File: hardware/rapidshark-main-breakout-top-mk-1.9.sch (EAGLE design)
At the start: 10 parts, among them U1 ADAFRUIT_METRO_MININOSILK-AMB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

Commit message: tweaks to jst part hole sizes
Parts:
- F1: value 100mA -> 120mA
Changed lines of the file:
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@@
 <setting verticaltext="up"/>
 </settings>
-<grid distance="100" unitdist="mil" unit="mil" style="lines" multiple="1" display="yes" altdistance="1" altunitdist="mil" altunit="mil"/>
+<grid distance="100" unitdist="mil" unit="mil" style="lines" multiple="1" display="yes" altdistance="2" altunitdist="mil" altunit="mil"/>
 <layers>
 <layer number="1" name="Top" color="4" fill="1" visible="no" active="no"/>
@@
 <part name="SUPPLY16" library="A_butts" deviceset="5V" device=""/>
 <part name="SUPPLY17" library="A_butts" deviceset="3.3V" device=""/>
-<part name="F1" library="A_butts" deviceset="PTC" device="SMD" value="100mA"/>
+<part name="F1" library="A_butts" deviceset="PTC" device="SMD" value="120mA"/>
 <part name="SUPPLY1" library="A_butts" deviceset="5V" device=""/>
 <part name="SUPPLY2" library="A_butts" deviceset="5V" device=""/>

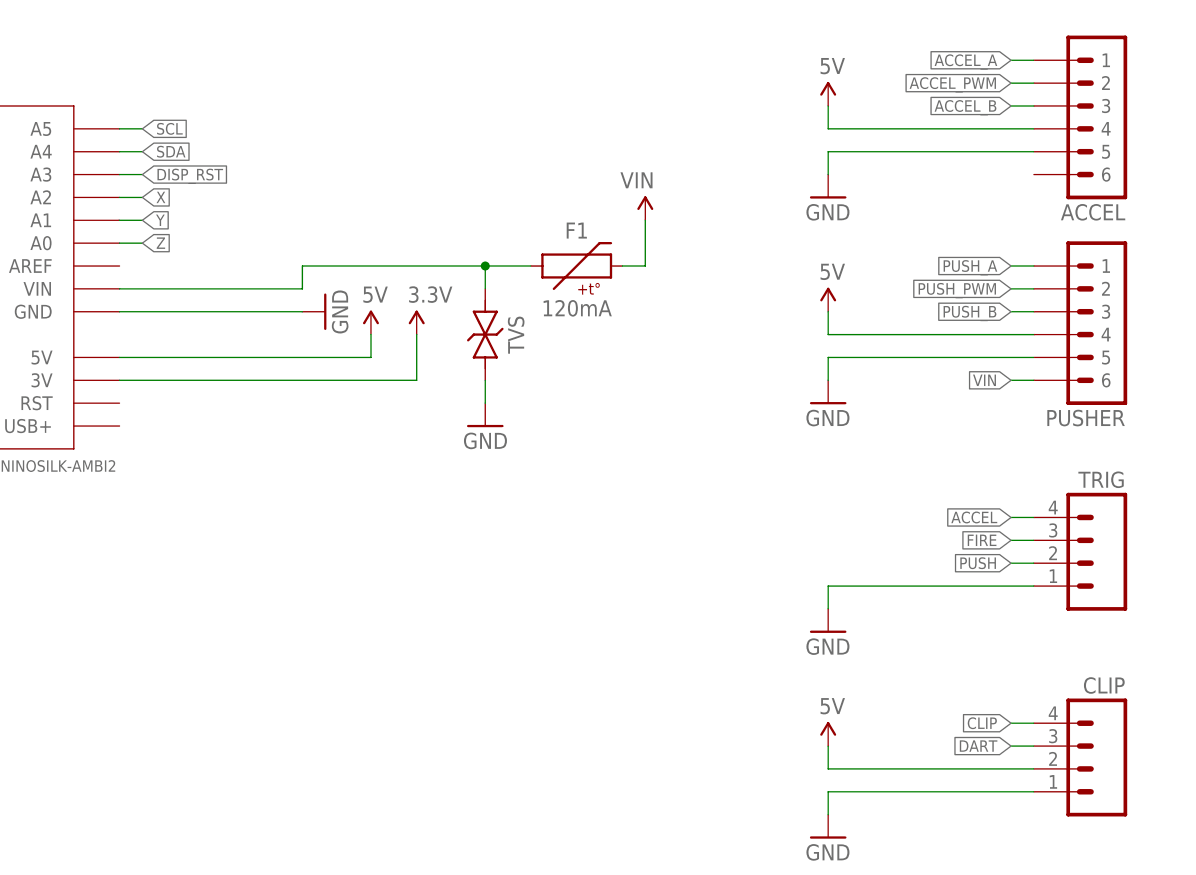
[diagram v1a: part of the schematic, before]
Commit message: relayout and now provides both 3V and 5V to display (but assumes IO voltage is whatever the arduino sends out
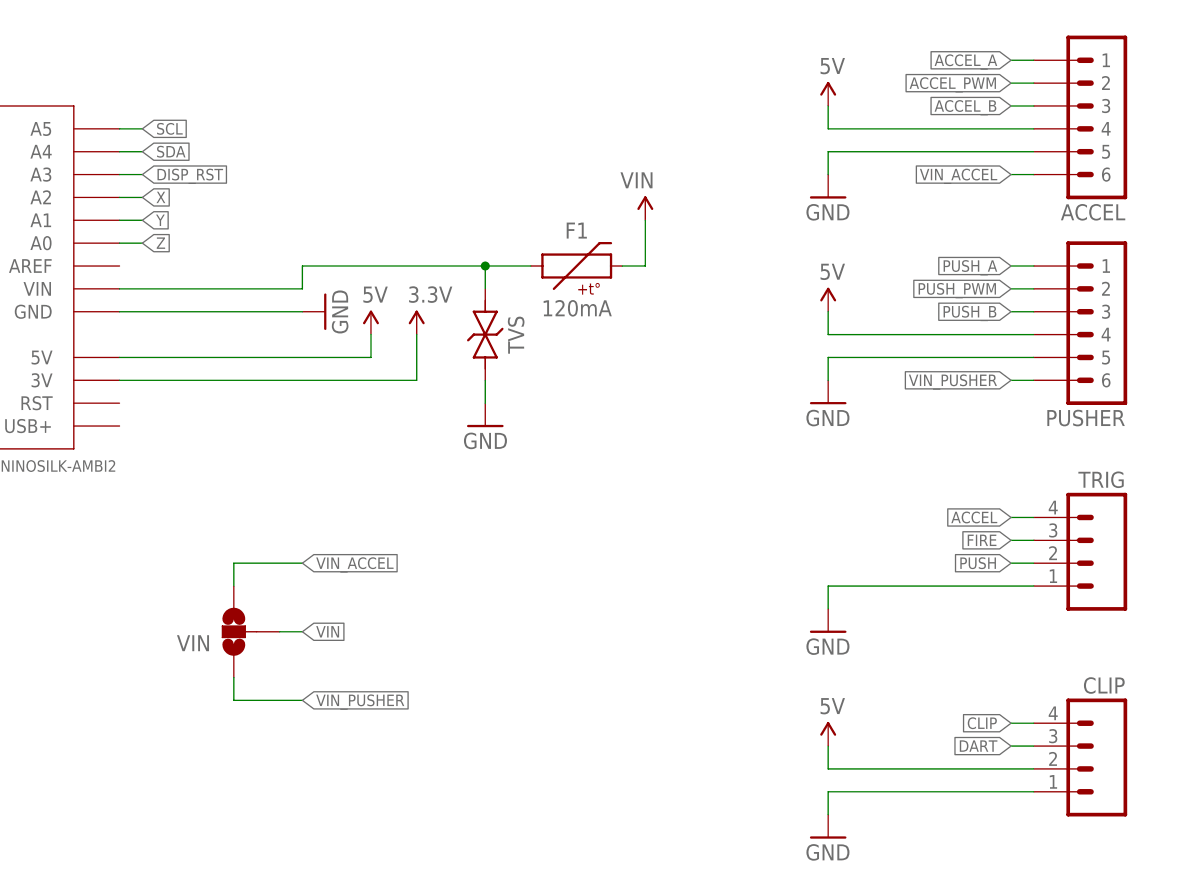
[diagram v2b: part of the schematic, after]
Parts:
- added VIN: (no value), A_butts:JUMPER-PAD-3-NOFULL_BOX_SILK
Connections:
- new net VIN_ACCEL: ACCEL.6, VIN.3
- new net VIN_PUSHER: PUSHER.6, VIN.1
- net VIN: now also VIN.2; no longer PUSHER.6
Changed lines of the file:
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@@
 <part name="GND7" library="A_butts" deviceset="GND" device=""/>
 <part name="DSPLY" library="A_butts" deviceset="M06" device="JST-PH-PTH-VERT"/>
+<part name="VIN" library="A_butts" deviceset="JUMPER-PAD-3-NO" device="FULL_BOX_SILK"/>
 </parts>
 <sheets>
@@
 <instance part="GND7" gate="1" x="152.4" y="43.18"/>
 <instance part="DSPLY" gate="G$1" x="177.8" y="53.34" rot="MR0"/>
+<instance part="VIN" gate="G$1" x="83.82" y="96.52" rot="R180"/>
 </instances>
 <busses>
@@
 </segment>
 <segment>
-<wire x1="170.18" y1="124.46" x2="172.72" y2="124.46" width="0.1524" layer="91"/>
-<label x="170.18" y="124.46" size="1.27" layer="95" rot="R180" xref="yes"/>
-<pinref part="PUSHER" gate="G$1" pin="6"/>
+<pinref part="VIN" gate="G$1" pin="2"/>
+<wire x1="88.9" y1="96.52" x2="91.44" y2="96.52" width="0.1524" layer="91"/>
+<label x="91.44" y="96.52" size="1.27" layer="95" xref="yes"/>
 </segment>
 </net>
@@
 </segment>
 </net>
+<net name="VIN_PUSHER" class="0">
+<segment>
+<wire x1="170.18" y1="124.46" x2="172.72" y2="124.46" width="0.1524" layer="91"/>
+<label x="170.18" y="124.46" size="1.27" layer="95" rot="R180" xref="yes"/>
+<pinref part="PUSHER" gate="G$1" pin="6"/>
+</segment>
+<segment>
+<pinref part="VIN" gate="G$1" pin="1"/>
+<wire x1="83.82" y1="91.44" x2="83.82" y2="88.9" width="0.1524" layer="91"/>
+<wire x1="83.82" y1="88.9" x2="91.44" y2="88.9" width="0.1524" layer="91"/>
+<label x="91.44" y="88.9" size="1.27" layer="95" xref="yes"/>
+</segment>
+</net>
+<net name="VIN_ACCEL" class="0">
+<segment>
+<pinref part="ACCEL" gate="G$1" pin="6"/>
+<wire x1="170.18" y1="147.32" x2="172.72" y2="147.32" width="0.1524" layer="91"/>
+<label x="170.18" y="147.32" size="1.27" layer="95" rot="R180" xref="yes"/>
+</segment>
+<segment>
+<pinref part="VIN" gate="G$1" pin="3"/>
+<wire x1="83.82" y1="101.6" x2="83.82" y2="104.14" width="0.1524" layer="91"/>
+<wire x1="83.82" y1="104.14" x2="91.44" y2="104.14" width="0.1524" layer="91"/>
+<label x="91.44" y="104.14" size="1.27" layer="95" xref="yes"/>
+</segment>
+</net>
